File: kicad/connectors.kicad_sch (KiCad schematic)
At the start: 43 parts, among them J1 USB4105-GF-A, J2 ESC, J3 HD VTX, J4 GPS, J5 ELRS, P13 5V, P14 BUZ_N, P15 UART5_TX, P16 UART5_RX, P17 UART6_TX, P18 UART6_RX, P19 MOTOR5, P20 MOTOR6, P21 MOTOR7, P22 MOTOR8, P23 RSSI_IN, P24 GND, P25 5V, Q1 PMV40UN2, U13 USBLC6-2SC6

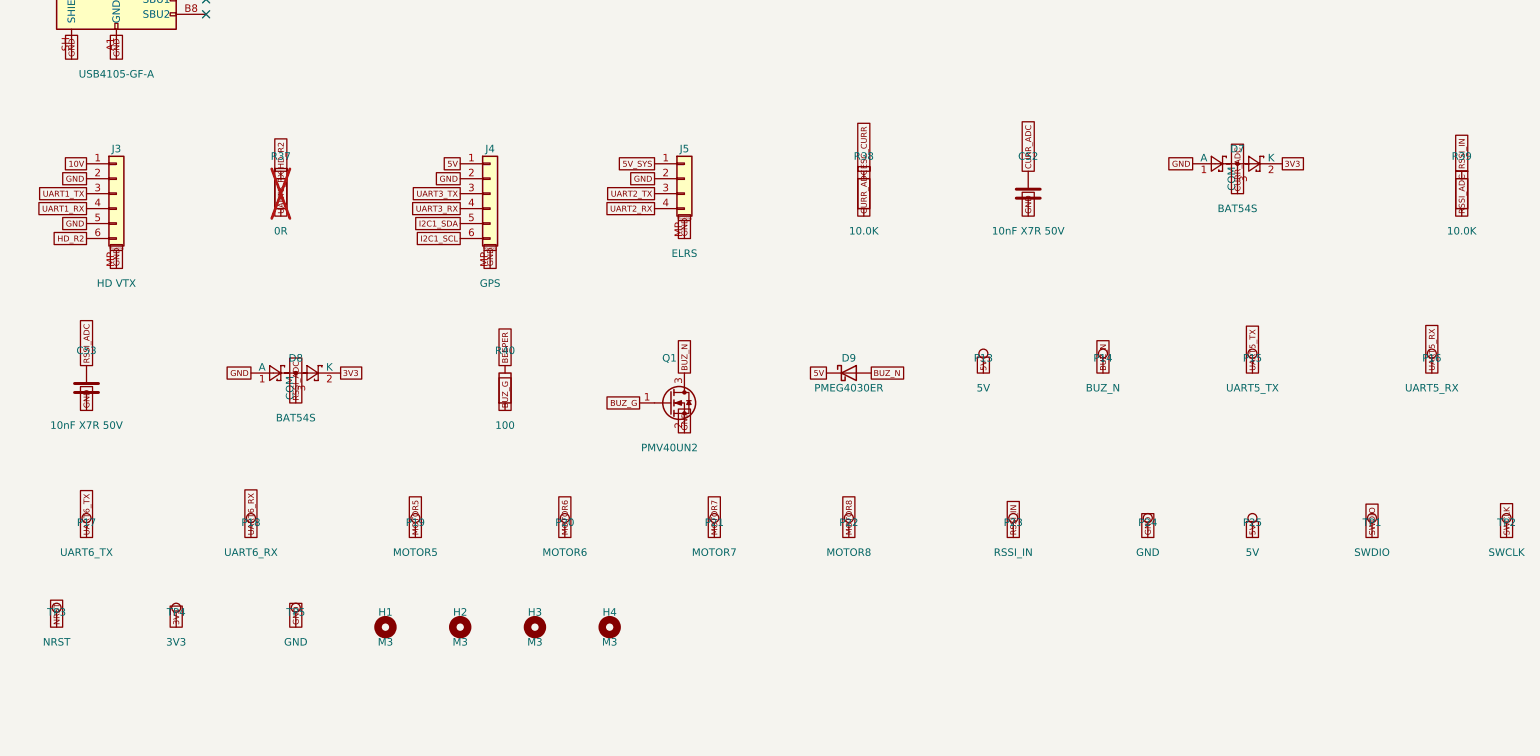
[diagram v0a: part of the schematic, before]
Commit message: Gate 1 fixes (crystal gm evidence, LDO output ESR, X7R caps, 50V HF cap, per-MPN datasheets, in_bom flags, project-file merge, parity fields), power re-audit fixes (board-level thermal envelope, USB inrush deviation, R41 VTX 0R link), PCB placement + legalizer + grommet keepouts; Gate 1 reports
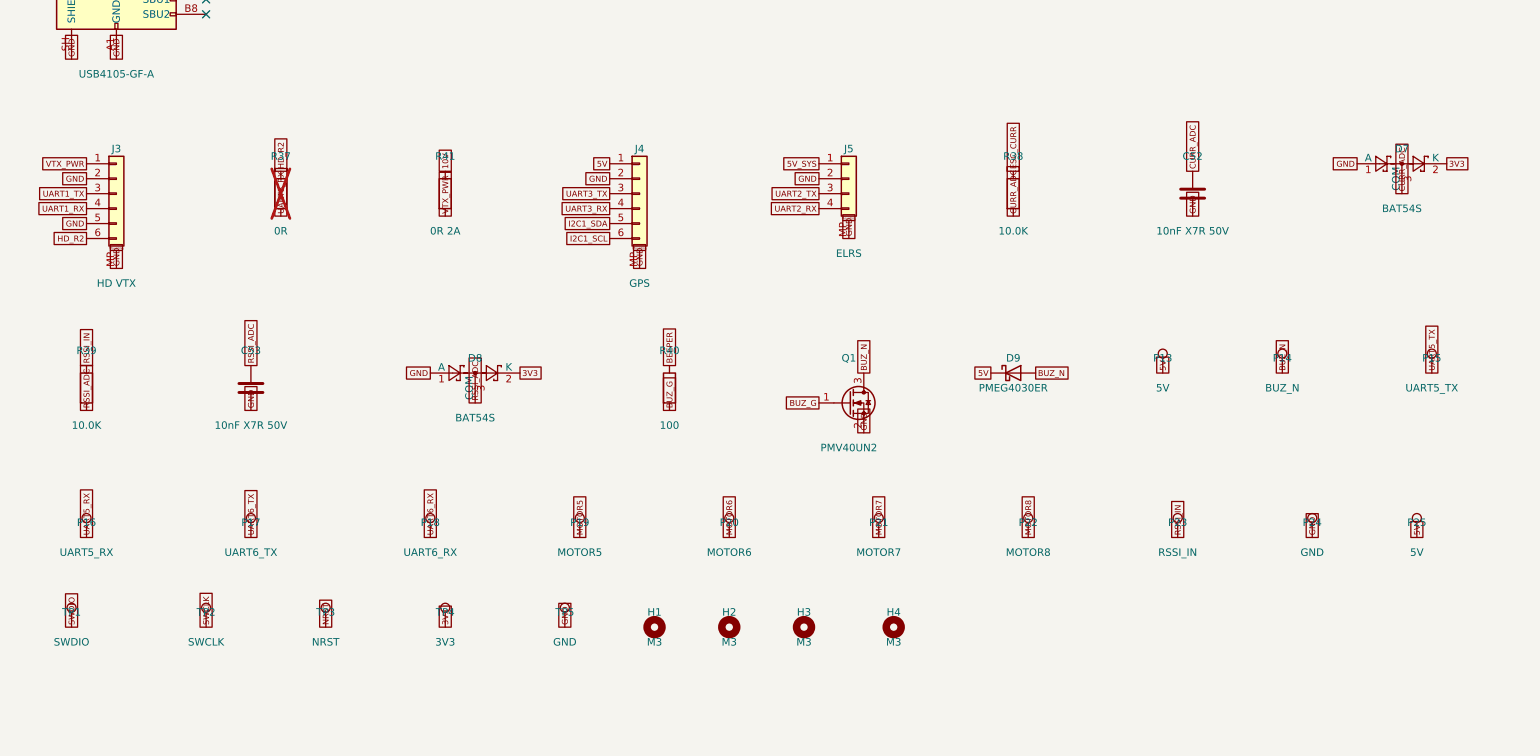
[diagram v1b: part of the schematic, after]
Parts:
- added R41: 0R 2A, Resistor_SMD:R_0805_2012Metric, symbol Device:R
- H1, H2, H3, H4: footprint MountingHole:MountingHole_3.2mm_M3 -> F405FC:MountingHole_3.2mm_M3_Grommet4.6mm; now left out of the parts list
- P13, P14, P15, P16, P17, P18, P19, P20, P21, P22, P23, P24, P25, TP1, TP2, TP3, TP4, TP5: now left out of the parts list
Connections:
- net 10V: now also R41.1; no longer J3.1 (Pin_1)
- new net VTX_PWR: J3.1 (Pin_1), R41.2
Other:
- moved on the sheet: C52, C53, D7, D8, D9, H1, H2, H3, H4, J4, J5, P13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

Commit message: Gate 2 sourcing: apply DigiKey drop-in replacements (G2S-01/02/03/09), PN corrections, regenerate BOM; sourcing report and DigiKey BOM CSVs
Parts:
- C52, C53: DigiKey 1276-1015-1-ND (verify) -> 1276-1028-1-ND
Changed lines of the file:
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@@
 			)
 		)
-		(property "DigiKey" "1276-1015-1-ND (verify)"
+		(property "DigiKey" "1276-1028-1-ND"
 			(at 215.9 91.44 0)
 			(effects
@@
 			)
 		)
-		(property "DigiKey" "1276-1015-1-ND (verify)"
-			(at 55.88 124.46 0)
-			(effects
+		(property "DigiKey" "1276-1028-1-ND"
+			(at 55.88 124.46 0)
+			(effects

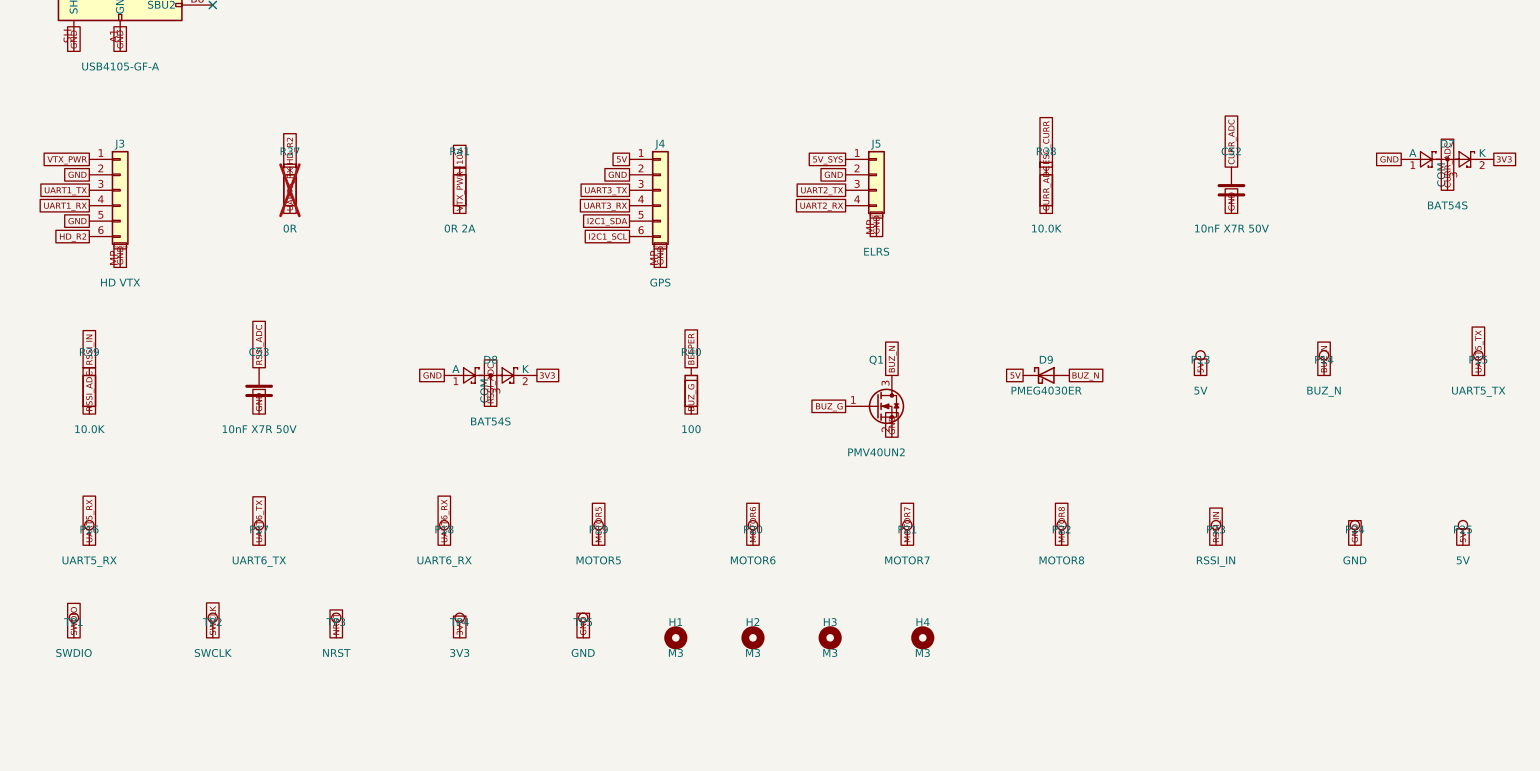
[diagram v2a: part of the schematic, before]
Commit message: D-23: ADC clamp diodes removed (routing space under the MCU corner); BOM $174.68; PathFinder RESET_NETS
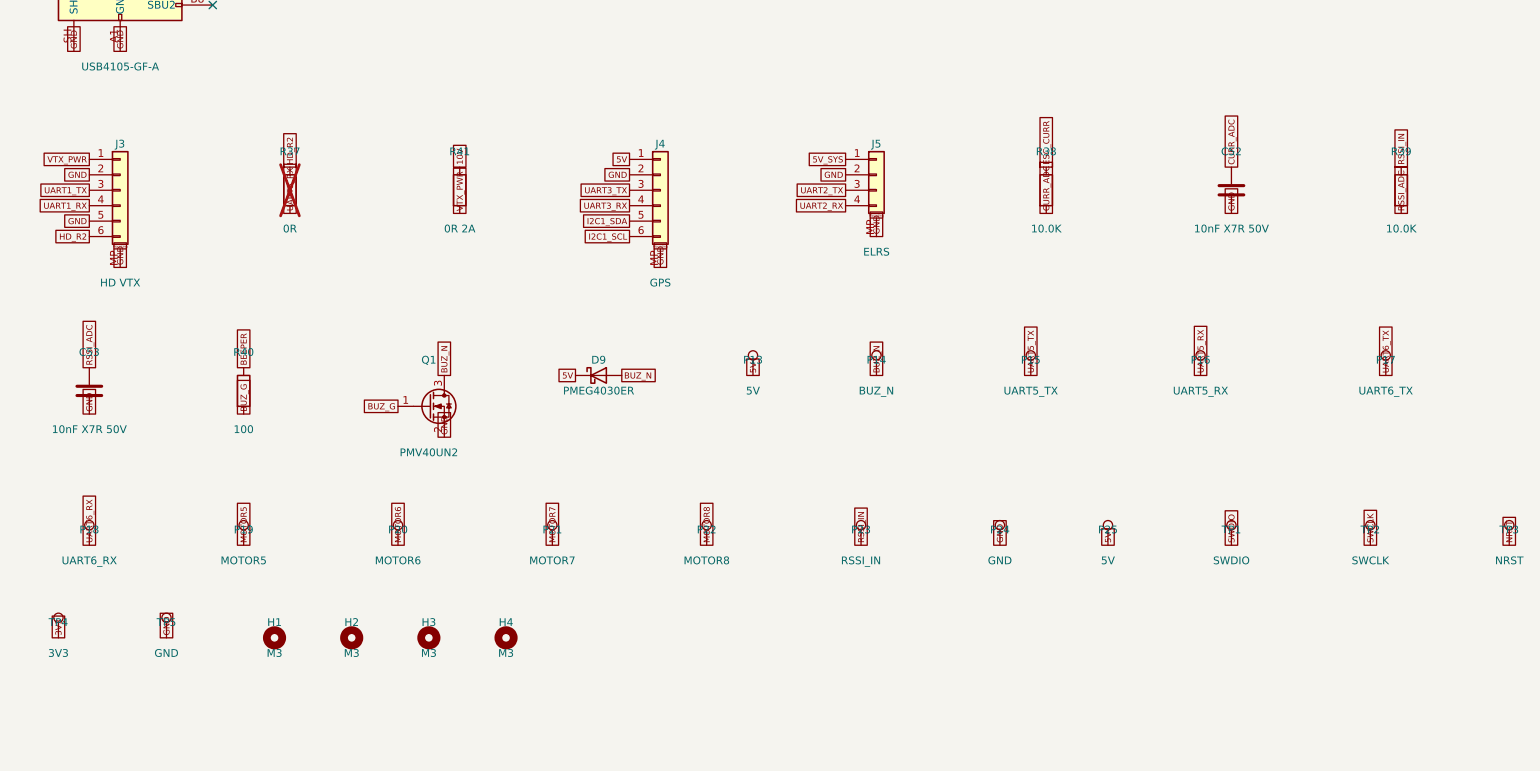
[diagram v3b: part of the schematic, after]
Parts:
- removed D7, D8: BAT54S, Package_TO_SOT_SMD:SOT-23, symbol Diode:BAT54S
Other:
- moved on the sheet: C53, D9, H1, H2, H3, H4, P13, P14, P15, P16, P17, P18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

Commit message: Readable schematic: functional blocks with titles, passives wired to their IC pins, GND power symbols, per-rail decoupling banks, labels only between blocks (ERC 0, netcheck OK, same nets)
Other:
- note added: "CURR_ADC decoupling / bulk"
- note added: "J1 USB4105-GF-A - USB-C (USB 2.0 FS)"
- note added: "J2 ESC - ESC: VBAT GND CURR M1 M2 M3 M4 TLM"
- note added: "J3 HD VTX - HD VTX: 10V GND TX RX GND SBUS/R2"
- note added: "J4 GPS - GPS: 5V GND TX RX SDA SCL"
- note added: "J5 ELRS - ELRS RX: 5V GND TX RX"
- note added: "RSSI_ADC decoupling / bulk"
- note added: "U13 USBLC6-2SC6 - USB ESD"
- moved on the sheet: C51, C52, C53, D4, D9, H1, H2, H3, H4, J1, J2, J3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
